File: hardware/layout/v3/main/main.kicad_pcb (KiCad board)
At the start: 4 copper layers, 39.8 x 78 mm, 75 parts, among them J1 KNX bus terminal pins, J2 AUX 20-32 V (yellow/white), J3 DALI bus (push-in), J4 UI board, Q1 MJD45H11, Q2 BC857, Q3 IRLML0060, Q4 BC847, Q5 BC847, Q6 BC847, U1 NCN5130MNTWG, U2 SCT2400TVBR, U3 REM3-2415S/A/CTRL 24V->15V 3W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, U4 TLP383, U5 TLP383(D4BLLTL,E, U6 TLP383(D4BLLTL,E, U7 LM66100, U8 XIAO ESP32C6, Y1 16MHz

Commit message: Updated DALI DC-DC converter from RECOM REM3-2415S/A to REC3-2415SRW/H2/A series across all variants, changed V3 OLED from 14-pin 0.5mm ZIF to 14-pin 0.62mm solder-tail FPC connector, and expanded assembly documentation with Mouser/Digi-Key/TME part numbers and alternative suppliers
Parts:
- U3: value REM3-2415S/A/CTRL 24V->15V 3W iso -> REC3-2415SRW/H2/A/CTRL 24V->15V 3W iso

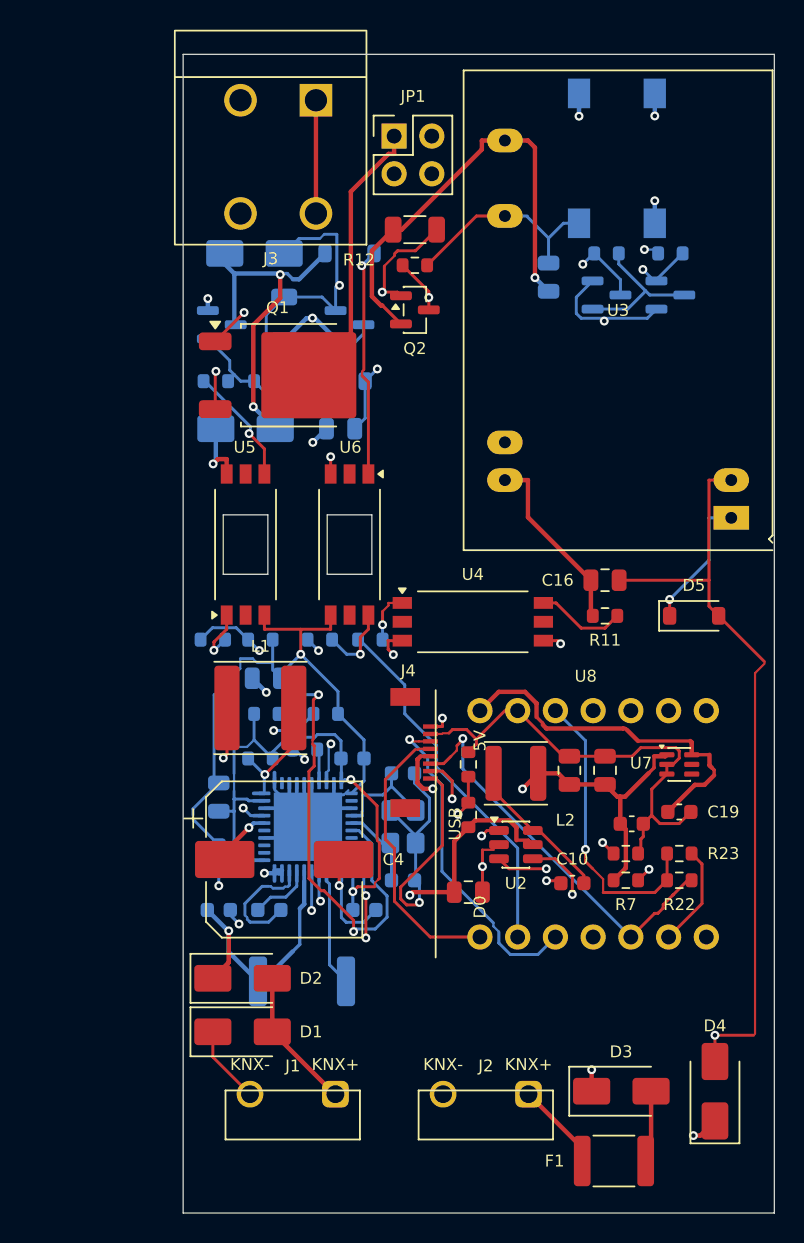
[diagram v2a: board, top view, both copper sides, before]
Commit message: Removed V1 hardware variant from CI workflows, updated AGENTS.md documentation to reflect V2/V3-only support
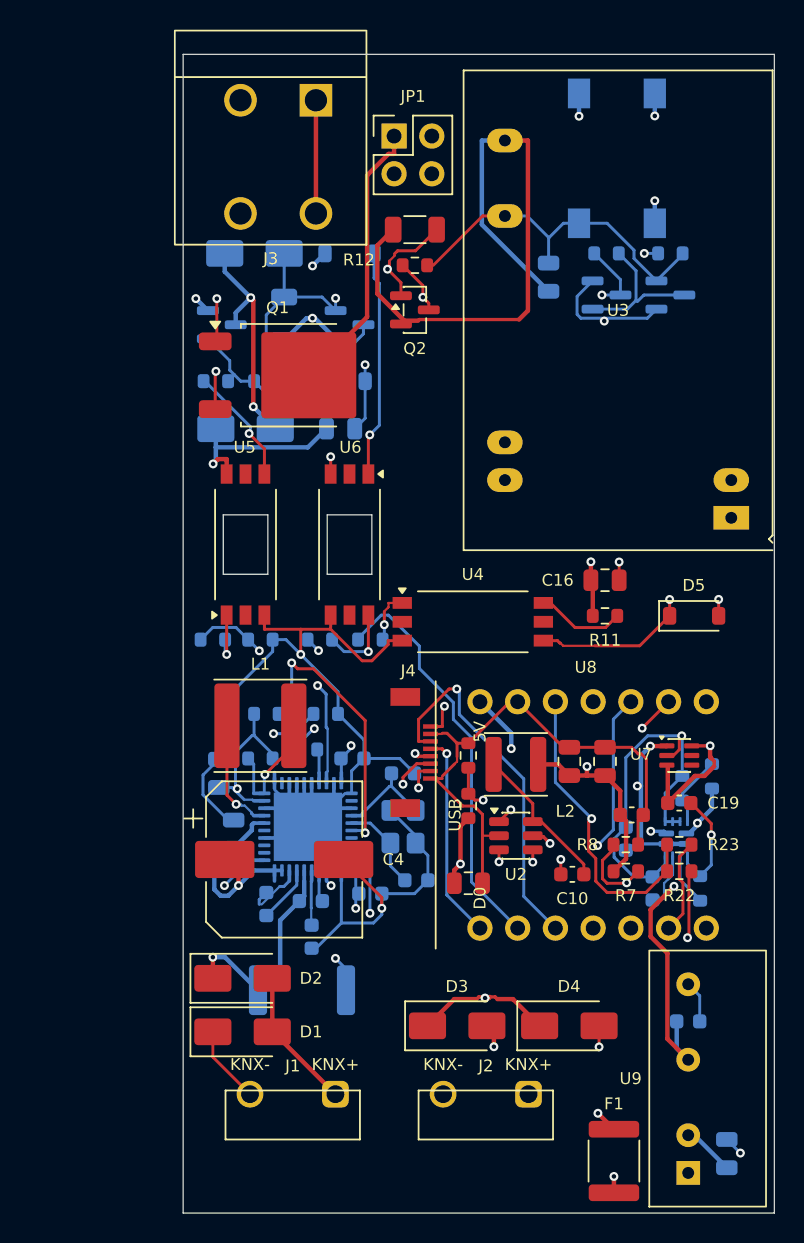
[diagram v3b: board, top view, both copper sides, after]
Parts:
- added C20: 10u 50V, Capacitor_SMD:C_0805_2012Metric, B.Cu at (36.6, -4.00)
- added C21: 10u 10V, Capacitor_SMD:C_0603_1608Metric, B.Cu at (34.0, -12.9)
- added C22: 100n 50V, Capacitor_SMD:C_0603_1608Metric, B.Cu at (31.6, -21.9)
- added C23: 10u 10V, Capacitor_SMD:C_0603_1608Metric, B.Cu at (29.8, -25.2)
- added R24: 30k, Resistor_SMD:R_0603_1608Metric, B.Cu at (35.6, -29.4)
- added R25: 10k, Resistor_SMD:R_0603_1608Metric, B.Cu at (33.6, -28.6)
- added R26: 100k 1%, Resistor_SMD:R_0603_1608Metric, B.Cu at (34.8, -21.9)
- added U10: TPS2121RUXR, Package_DFN_QFN:Texas_VQFN-HR-12_2x2.5mm_P0.5mm, B.Cu at (33.2, -25.2)
- added U9: TMR 1-2411 24V->5V 1W iso, gateway_fp:Converter_DCDC_TRACO_TMR1_SIP6, F.Cu at (34.0, -2.70)
- R16: value 22k -> 4k7
- R17: value 100k -> 10k
- R18: value 3R3 -> 2R
- R21: value 10k -> 4k7
- R5: value 120k 1% -> 100k 1%
- moved D3 11.9 mm to (18.4, -12.6)
- moved D4 10.7 mm to (26.0, -12.6), turned to 0 degrees
- moved C15 10.7 mm to (3.40, -25.5), turned to 90 degrees
- moved C2 8.26 mm to (8.65, -18.6), turned to -90 degrees
- moved C1 6.23 mm to (8.60, -21.0)
- moved C7 1.60 mm to (2.40, -29.6)
- moved L1 1.20 mm to (5.20, -32.8)
- moved C5 1.17 mm to (12.6, -21.5)
- moved C8 0.90 mm to (15.7, -22.4)
- moved C10 0.60 mm to (26.2, -22.8)
- moved C14 0.60 mm to (30.2, -26.8)
- moved C19 0.60 mm to (33.4, -27.6)
- moved R22 0.60 mm to (33.4, -23.0)
- moved R23 0.60 mm to (33.4, -24.8)
- moved R6 0.60 mm to (19.2, -30.8)
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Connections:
- C12 pad 1: +5V -> +5V_BUCK
- C13 pad 1: +5V -> +5V_BUCK
- C14 pad 1: +5V -> +5V_BUCK
- L2 pad 2: +5V -> +5V_BUCK
- R7 pad 1: +5V -> +5V_BUCK
- U7 pad 3: GND -> +5V_XIAO
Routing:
- net GND: track 139.6 -> 185.4 mm, vias 5 -> 4
- net +5V_AUX: track 0.00 -> 25.0 mm, vias 0 -> 2
- net +5V_BUCK: track 0.00 -> 20.1 mm, vias 0 -> 2
- net DALI_ISO15V: track 30.4 -> 42.8 mm, vias 1 -> 0
- net AUX_P: track 83.1 -> 95.0 mm
- net +3V3_TRX: track 39.5 -> 51.2 mm, vias 2 -> 4
- net DALI_TX: track 41.3 -> 30.6 mm
- net +5V: track 28.3 -> 37.0 mm, vias 2 -> 3
- net I2C_SDA: track 27.0 -> 34.8 mm, vias 1 -> 2
- net CCP: track 9.96 -> 2.16 mm, vias 2 -> 0
- net AUX_FUSED: track 4.85 -> 12.2 mm, vias 0 -> 2
- net CAV: track 10.8 -> 3.73 mm, vias 2 -> 0
- net GNDA: track 50.9 -> 44.2 mm, vias 1 -> 4
- net NCN_SAVEB: track 54.4 -> 47.8 mm, vias 2 -> 3
- net KNX_TXD: track 30.2 -> 35.5 mm
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
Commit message: Updated AUX-to-core converter from 1W TMR 1-2411 to 2W TMR 2411 (v3) and 3W TRN 3-2411 (v2) to handle WiFi TX peaks without KNX handover, relocated v3 converter to front protrusion tongue with AUX feed corridor along board edges, increased core hold-up capacitor C23 to 100µF 1206, added board slot between TRN3 pins 2/3 for creepage, updated domain regions and copper keepouts for new layouts, and added DCDC_SIP5/DCDC_SIP8_REMOTE symbols with converter parameter support in core_power.build()
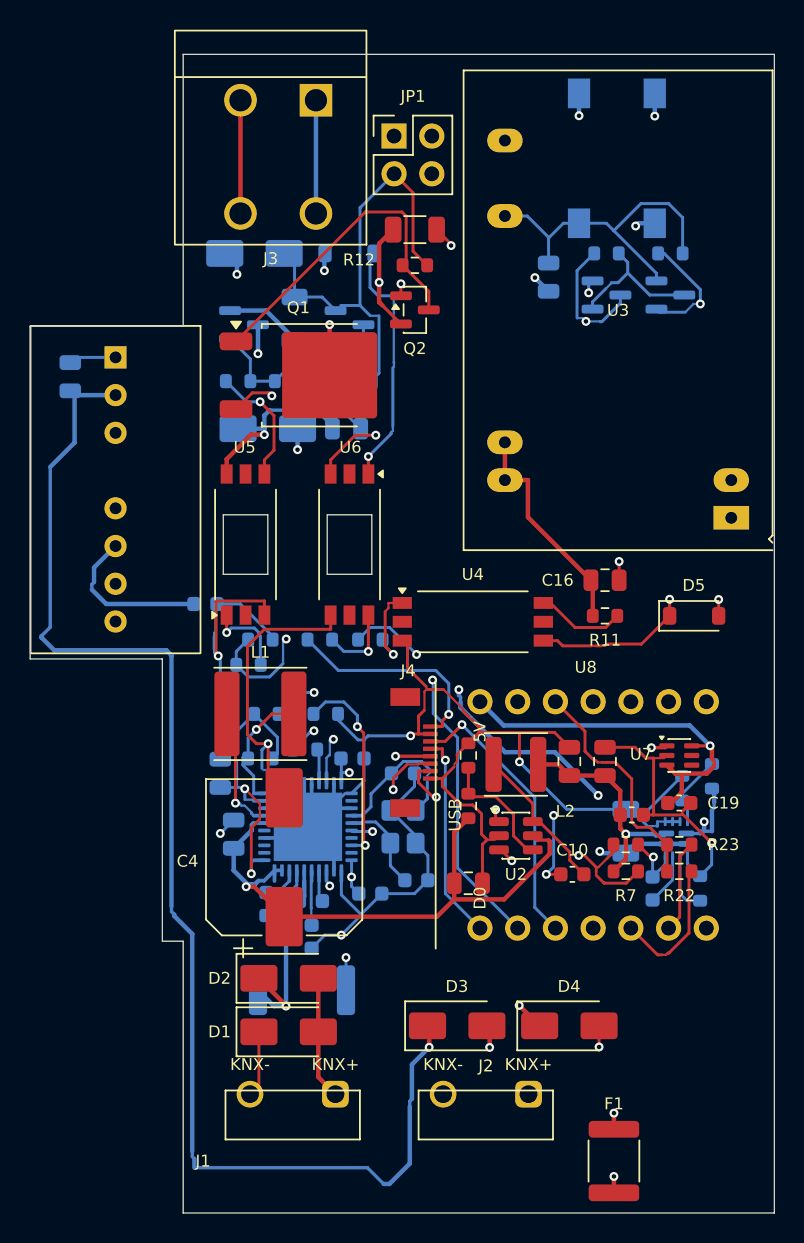
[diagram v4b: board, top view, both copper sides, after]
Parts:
- C23: value 10u 10V -> 100u 6.3V; footprint Capacitor_SMD:C_0603_1608Metric -> Capacitor_SMD:C_1206_3216Metric
- U9: value TMR 1-2411 24V->5V 1W iso -> TMR 2411 24V->5V 2W iso; footprint gateway_fp:Converter_DCDC_TRACO_TMR1_SIP6 -> gateway_fp:Converter_DCDC_TRACO_TMR2_SIP8
- moved C20 68.5 mm to (-7.60, -56.3)
- moved U9 67.1 mm to (-4.55, -57.6), turned to -90 degrees
- moved C21 43.0 mm to (1.50, -41.0)
- moved D1 3.10 mm to (7.10, -12.2)
- moved D2 3.10 mm to (7.10, -15.8)
- moved R14 2.94 mm to (4.40, -36.9)
- moved D8 1.50 mm to (5.70, -52.8)
- moved R16 1.50 mm to (3.70, -56.0)
- moved Q3 1.50 mm to (4.10, -59.8)
- moved R17 1.40 mm to (7.00, -56.0)
- moved Q1 1.40 mm to (8.60, -56.4)
- moved L1 0.80 mm to (5.20, -33.6)
- moved R18 0.70 mm to (7.50, -60.2)
- moved C23 0.50 mm to (29.8, -25.7)
- moved C18 0.40 mm to (11.0, -52.8)
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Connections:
- U9 pad 6: GND -> +5V_AUX
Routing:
- net GNDA: track 44.2 -> 132.8 mm, vias 4 -> 3
- net AUX_P: track 95.0 -> 175.7 mm
- net +5V_AUX: track 25.0 -> 68.6 mm, vias 2 -> 3
- net GND: track 185.4 -> 159.6 mm, vias 4 -> 8
- net FANIN: track 35.2 -> 13.6 mm
- net GNDD: track 42.2 -> 61.7 mm, vias 2 -> 0
- net DALI_RX: track 46.3 -> 29.9 mm, vias 2 -> 1
- net DALI_ISO15V: track 42.8 -> 30.9 mm, vias 0 -> 2
- net +3V3_TRX: track 51.2 -> 39.7 mm
- net DA_P: track 48.1 -> 57.5 mm, vias 4 -> 5
- net DALI_SENSE: track 14.2 -> 8.04 mm, vias 2 -> 0
- net BTN_LADDER: track 24.6 -> 18.9 mm
- net KNX_TXD: track 35.5 -> 30.2 mm
- net +5V_BUCK: track 20.1 -> 15.0 mm, vias 2 -> 1
- net +3V3: track 42.8 -> 38.5 mm, vias 3 -> 1
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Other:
- board size 39.8 x 78 mm -> 50.1 x 78 mm

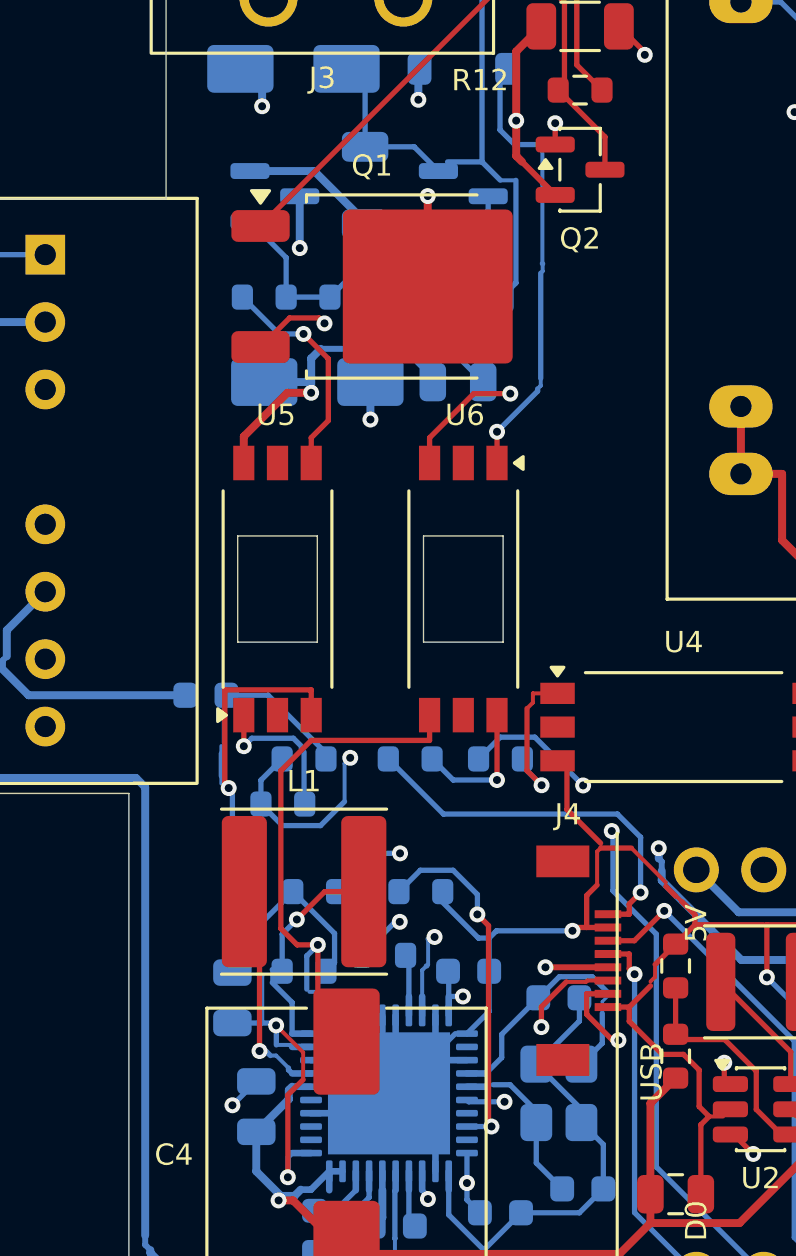
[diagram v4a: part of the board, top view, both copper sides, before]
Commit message: Added zero-length track segments to fix hairline joints where track ends grazed pads instead of fully entering them
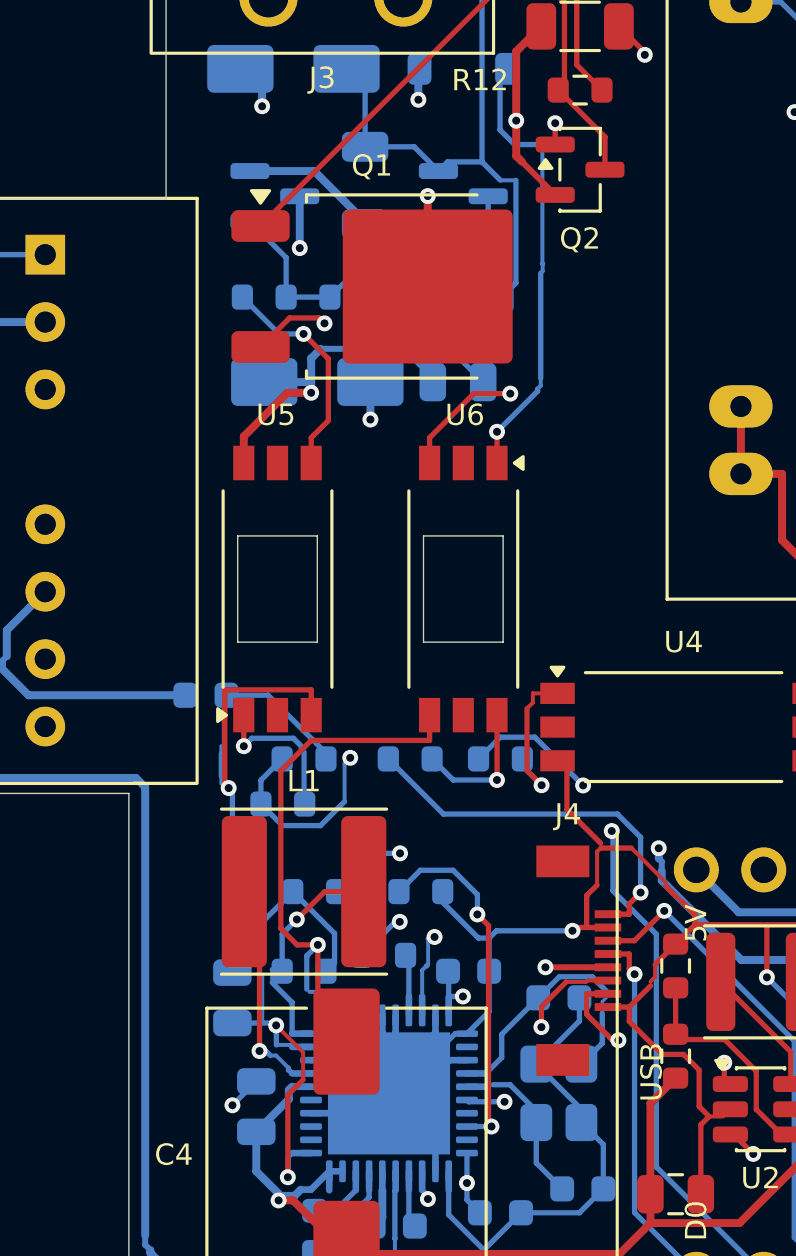
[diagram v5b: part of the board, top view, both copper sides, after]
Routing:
- net GND: track 159.6 -> 175.7 mm
